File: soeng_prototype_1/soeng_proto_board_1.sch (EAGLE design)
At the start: 11 parts, among them J1 2172034-1

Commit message: PCB Rev. 2
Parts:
- removed CN1: (no value), adafruit:JST_2PIN-THM-RA
- added R1: 10, adafruit:R-US_0207/9
- added SPKR+, SPKR-: WIREPAD1,6/0,8, wirepad:WIREPAD1,6/0,8
- added T1: 2N2222, adafruit:2N2222
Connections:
- new net N$9: R1.1, SPKR+.P
- net +5V: now also T1.C
- net GND: now also SPKR-.P
- net N$4: now also T1.B; no longer CN1.2
- net N$6: now also R1.2, T1.E; no longer CN1.1, U$1.AUD_N
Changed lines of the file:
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@@
 <part name="J1" library="TE-Mini-USB" deviceset="2172034-1" device=""/>
 <part name="LED_STRIP" library="pinhead" library_urn="urn:adsk.eagle:library:325" deviceset="PINHD-1X3" device="" package3d_urn="urn:adsk.eagle:package:22458/2"/>
-<part name="CN1" library="adafruit" library_urn="urn:adsk.eagle:library:420" deviceset="JST_2PIN" device="-THM-RA" package3d_urn="urn:adsk.eagle:package:6240694/1"/>
 <part name="U$2" library="lap_2019" deviceset="RDI-PUSHBUTTON" device=""/>
 <part name="U$3" library="lap_2019" deviceset="RDI-PUSHBUTTON" device=""/>
@@
 <part name="C4" library="adafruit" library_urn="urn:adsk.eagle:library:420" deviceset="C-US" device="025-025X050" package3d_urn="urn:adsk.eagle:package:6240323/1"/>
 <part name="DOT_MATRIX_DISPLAY" library="pinhead" library_urn="urn:adsk.eagle:library:325" deviceset="PINHD-1X5" device="" package3d_urn="urn:adsk.eagle:package:22469/2"/>
+<part name="T1" library="adafruit" library_urn="urn:adsk.eagle:library:420" deviceset="2N2222" device="" package3d_urn="urn:adsk.eagle:package:6240647/1"/>
+<part name="SPKR+" library="wirepad" library_urn="urn:adsk.eagle:library:412" deviceset="WIREPAD" device="1,6/0,8" package3d_urn="urn:adsk.eagle:package:30830/1"/>
+<part name="SPKR-" library="wirepad" library_urn="urn:adsk.eagle:library:412" deviceset="WIREPAD" device="1,6/0,8" package3d_urn="urn:adsk.eagle:package:30830/1"/>
+<part name="R1" library="adafruit" library_urn="urn:adsk.eagle:library:420" deviceset="R-US_" device="0207/9" package3d_urn="urn:adsk.eagle:package:6240935/1" value="10"/>
 </parts>
 <sheets>
@@
 <attribute name="VALUE" x="3.81" y="35.56" size="1.778" layer="96" rot="R180"/>
 </instance>
-<instance part="CN1" gate="G$1" x="-2.54" y="12.7" smashed="yes" rot="R180">
-<attribute name="NAME" x="3.81" y="6.985" size="1.778" layer="95" rot="R180"/>
-<attribute name="VALUE" x="3.81" y="17.78" size="1.778" layer="96" rot="R180"/>
-</instance>
 <instance part="U$2" gate="G$1" x="35.56" y="-10.16" smashed="yes"/>
 <instance part="U$3" gate="G$1" x="35.56" y="-38.1" smashed="yes"/>
@@
 <attribute name="NAME" x="3.81" y="37.465" size="1.778" layer="95" rot="R180"/>
 <attribute name="VALUE" x="3.81" y="55.88" size="1.778" layer="96" rot="R180"/>
+</instance>
+<instance part="T1" gate="G$1" x="12.7" y="0" smashed="yes">
+<attribute name="NAME" x="2.54" y="7.62" size="1.778" layer="95"/>
+<attribute name="VALUE" x="2.54" y="5.08" size="1.778" layer="96"/>
+</instance>
+<instance part="SPKR+" gate="G$1" x="15.24" y="-22.86" smashed="yes" rot="R90">
+<attribute name="NAME" x="13.3858" y="-24.003" size="1.778" layer="95" rot="R90"/>
+<attribute name="VALUE" x="18.542" y="-24.003" size="1.778" layer="96" rot="R90"/>
+</instance>
+<instance part="SPKR-" gate="G$1" x="15.24" y="-30.48" smashed="yes" rot="R270">
+<attribute name="NAME" x="17.0942" y="-29.337" size="1.778" layer="95" rot="R270"/>
+<attribute name="VALUE" x="11.938" y="-29.337" size="1.778" layer="96" rot="R270"/>
+</instance>
+<instance part="R1" gate="G$1" x="15.24" y="-12.7" smashed="yes" rot="R90">
+<attribute name="NAME" x="13.7414" y="-16.51" size="1.778" layer="95" rot="R90"/>
+<attribute name="VALUE" x="18.542" y="-16.51" size="1.778" layer="96" rot="R90"/>
 </instance>
 </instances>
@@
 <junction x="104.14" y="10.16"/>
 </segment>
+<segment>
+<pinref part="SPKR-" gate="G$1" pin="P"/>
+<wire x1="15.24" y1="-33.02" x2="15.24" y2="-50.8" width="0.1524" layer="91"/>
+<label x="15.24" y="-53.34" size="1.778" layer="95"/>
+</segment>
 </net>
 <net name="+5V" class="0">
@@
 <junction x="114.3" y="17.78"/>
 </segment>
+<segment>
+<pinref part="T1" gate="G$1" pin="C"/>
+<wire x1="15.24" y1="5.08" x2="15.24" y2="7.62" width="0.1524" layer="91"/>
+<label x="15.24" y="7.62" size="1.778" layer="95"/>
+</segment>
 </net>
 <net name="N$5" class="0">
@@
 <net name="N$4" class="0">
 <segment>
-<pinref part="CN1" gate="G$1" pin="2"/>
 <wire x1="0" y1="12.7" x2="22.86" y2="12.7" width="0.1524" layer="91"/>
 <wire x1="22.86" y1="12.7" x2="22.86" y2="35.56" width="0.1524" layer="91"/>
 <pinref part="U$1" gate="G$1" pin="AUD_P"/>
 <wire x1="22.86" y1="35.56" x2="33.02" y2="35.56" width="0.1524" layer="91"/>
-</segment>
-</net>
-<net name="N$6" class="0">
-<segment>
-<pinref part="U$1" gate="G$1" pin="AUD_N"/>
-<wire x1="33.02" y1="33.02" x2="25.4" y2="33.02" width="0.1524" layer="91"/>
-<wire x1="25.4" y1="33.02" x2="25.4" y2="10.16" width="0.1524" layer="91"/>
-<pinref part="CN1" gate="G$1" pin="1"/>
-<wire x1="25.4" y1="10.16" x2="0" y2="10.16" width="0.1524" layer="91"/>
+<pinref part="T1" gate="G$1" pin="B"/>
+<wire x1="10.16" y1="0" x2="0" y2="0" width="0.1524" layer="91"/>
+<wire x1="0" y1="0" x2="0" y2="12.7" width="0.1524" layer="91"/>
 </segment>
 </net>
@@
 </segment>
 </net>
+<net name="N$6" class="0">
+<segment>
+<pinref part="T1" gate="G$1" pin="E"/>
+<pinref part="R1" gate="G$1" pin="2"/>
+<wire x1="15.24" y1="-7.62" x2="15.24" y2="-5.08" width="0.1524" layer="91"/>
+</segment>
+</net>
+<net name="N$9" class="0">
+<segment>
+<pinref part="R1" gate="G$1" pin="1"/>
+<pinref part="SPKR+" gate="G$1" pin="P"/>
+<wire x1="15.24" y1="-17.78" x2="15.24" y2="-20.32" width="0.1524" layer="91"/>
+</segment>
+</net>

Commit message: Rev. 3
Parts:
- removed SPKR+, SPKR-: WIREPAD1,6/0,8, wirepad:WIREPAD1,6/0,8
- added U$4: MICRO_SPKR, lap_2019:MICRO_SPKR
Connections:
- net GND: now also U$4.SPKR-; no longer SPKR-.P
- net N$9: now also U$4.SPKR+; no longer SPKR+.P
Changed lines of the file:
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@@
 <?xml version="1.0" encoding="utf-8"?>
 <!DOCTYPE eagle SYSTEM "eagle.dtd">
-<eagle version="9.5.2">
+<eagle version="9.6.2">
 <drawing>
 <settings>
@@
 <part name="DOT_MATRIX_DISPLAY" library="pinhead" library_urn="urn:adsk.eagle:library:325" deviceset="PINHD-1X5" device="" package3d_urn="urn:adsk.eagle:package:22469/2"/>
 <part name="T1" library="adafruit" library_urn="urn:adsk.eagle:library:420" deviceset="2N2222" device="" package3d_urn="urn:adsk.eagle:package:6240647/1"/>
-<part name="SPKR+" library="wirepad" library_urn="urn:adsk.eagle:library:412" deviceset="WIREPAD" device="1,6/0,8" package3d_urn="urn:adsk.eagle:package:30830/1"/>
-<part name="SPKR-" library="wirepad" library_urn="urn:adsk.eagle:library:412" deviceset="WIREPAD" device="1,6/0,8" package3d_urn="urn:adsk.eagle:package:30830/1"/>
 <part name="R1" library="adafruit" library_urn="urn:adsk.eagle:library:420" deviceset="R-US_" device="0207/9" package3d_urn="urn:adsk.eagle:package:6240935/1" value="10"/>
+<part name="U$4" library="lap_2019" deviceset="MICRO_SPKR" device=""/>
 </parts>
 <sheets>
@@
 <attribute name="VALUE" x="2.54" y="5.08" size="1.778" layer="96"/>
 </instance>
-<instance part="SPKR+" gate="G$1" x="15.24" y="-22.86" smashed="yes" rot="R90">
-<attribute name="NAME" x="13.3858" y="-24.003" size="1.778" layer="95" rot="R90"/>
-<attribute name="VALUE" x="18.542" y="-24.003" size="1.778" layer="96" rot="R90"/>
-</instance>
-<instance part="SPKR-" gate="G$1" x="15.24" y="-30.48" smashed="yes" rot="R270">
-<attribute name="NAME" x="17.0942" y="-29.337" size="1.778" layer="95" rot="R270"/>
-<attribute name="VALUE" x="11.938" y="-29.337" size="1.778" layer="96" rot="R270"/>
-</instance>
 <instance part="R1" gate="G$1" x="15.24" y="-12.7" smashed="yes" rot="R90">
 <attribute name="NAME" x="13.7414" y="-16.51" size="1.778" layer="95" rot="R90"/>
 <attribute name="VALUE" x="18.542" y="-16.51" size="1.778" layer="96" rot="R90"/>
 </instance>
+<instance part="U$4" gate="G$1" x="22.86" y="-53.34" smashed="yes"/>
 </instances>
 <busses>
@@
 </segment>
 <segment>
-<pinref part="SPKR-" gate="G$1" pin="P"/>
-<wire x1="15.24" y1="-33.02" x2="15.24" y2="-50.8" width="0.1524" layer="91"/>
-<label x="15.24" y="-53.34" size="1.778" layer="95"/>
+<pinref part="U$4" gate="G$1" pin="SPKR-"/>
+<wire x1="15.24" y1="-50.8" x2="15.24" y2="-58.42" width="0.1524" layer="91"/>
+<label x="12.7" y="-60.96" size="1.778" layer="95"/>
 </segment>
 </net>
@@
 <segment>
 <pinref part="R1" gate="G$1" pin="1"/>
-<pinref part="SPKR+" gate="G$1" pin="P"/>
-<wire x1="15.24" y1="-17.78" x2="15.24" y2="-20.32" width="0.1524" layer="91"/>
-</segment>
-</net>
+<pinref part="U$4" gate="G$1" pin="SPKR+"/>
+<wire x1="15.24" y1="-17.78" x2="15.24" y2="-43.18" width="0.1524" layer="91"/>
+</segment>
+</net>

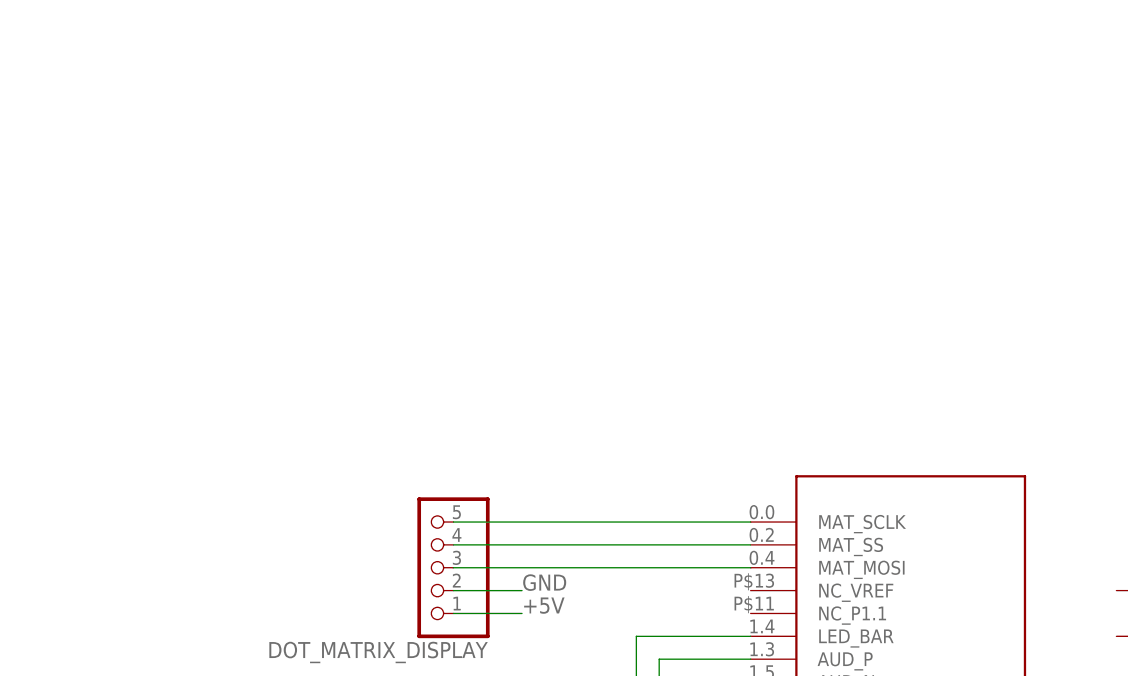
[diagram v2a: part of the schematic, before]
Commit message: Added TCXO, 3.3V Zener, RC
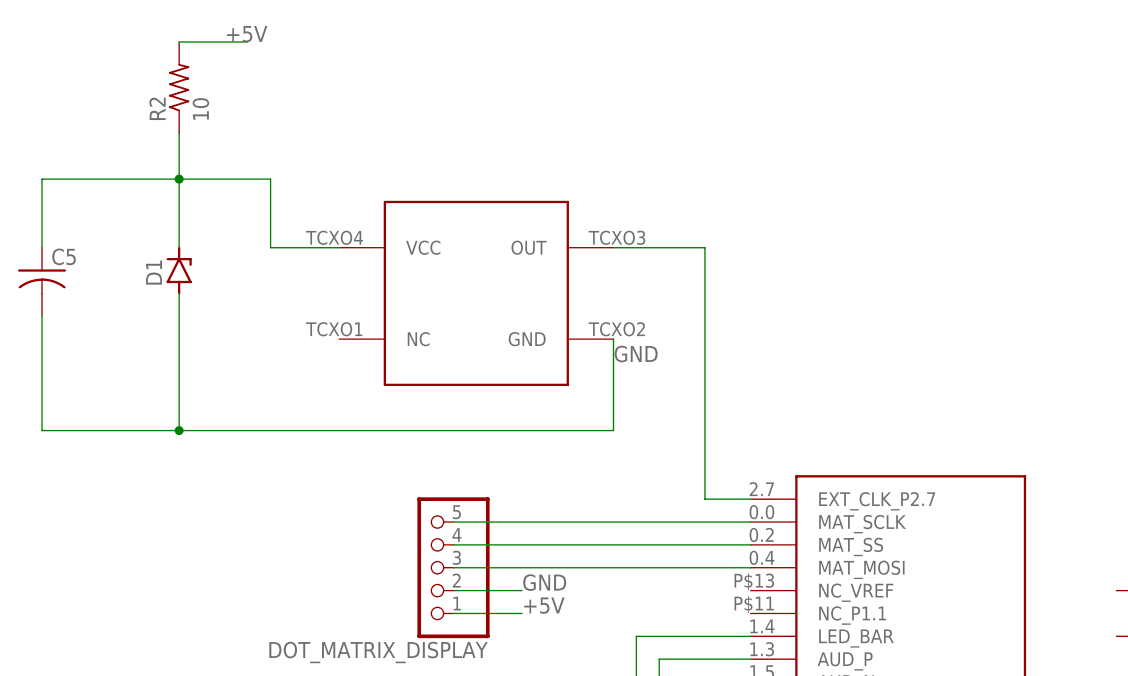
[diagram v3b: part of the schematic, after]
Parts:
- added C5: (no value), adafruit:C-US025-025X050
- added D1: (no value), diode:ZENER-DIODEDO34-7
- added R2: 10, adafruit:R-US_0207/9
- added U$5: TXEAPLSANF, lap_2019:TXEAPLSANF
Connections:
- new net N$10: U$1.EXT_CLK_P2.7, U$5.OUT
- new net N$11: C5.1, D1.C, R2.1, U$5.VCC
- net +5V: now also R2.2
- net GND: now also C5.2, D1.A, U$5.GND
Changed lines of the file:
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@@
 <part name="R1" library="adafruit" library_urn="urn:adsk.eagle:library:420" deviceset="R-US_" device="0207/9" package3d_urn="urn:adsk.eagle:package:6240935/1" value="10"/>
 <part name="U$4" library="lap_2019" deviceset="MICRO_SPKR" device=""/>
+<part name="U$5" library="lap_2019" deviceset="TXEAPLSANF" device=""/>
+<part name="D1" library="diode" library_urn="urn:adsk.eagle:library:210" deviceset="ZENER-DIODE" device="DO34-7" package3d_urn="urn:adsk.eagle:package:43364/1"/>
+<part name="R2" library="adafruit" library_urn="urn:adsk.eagle:library:420" deviceset="R-US_" device="0207/9" package3d_urn="urn:adsk.eagle:package:6240935/1" value="10"/>
+<part name="C5" library="adafruit" library_urn="urn:adsk.eagle:library:420" deviceset="C-US" device="025-025X050" package3d_urn="urn:adsk.eagle:package:6240323/1"/>
 </parts>
 <sheets>
@@
 </instance>
 <instance part="U$4" gate="G$1" x="22.86" y="-53.34" smashed="yes"/>
+<instance part="U$5" gate="G$1" x="2.54" y="76.2" smashed="yes"/>
+<instance part="D1" gate="G$1" x="-30.48" y="78.74" smashed="yes" rot="R90">
+<attribute name="NAME" x="-32.385" y="76.962" size="1.778" layer="95" rot="R90"/>
+<attribute name="VALUE" x="-27.051" y="76.962" size="1.778" layer="96" rot="R90"/>
+</instance>
+<instance part="R2" gate="G$1" x="-30.48" y="99.06" smashed="yes" rot="R90">
+<attribute name="NAME" x="-31.9786" y="95.25" size="1.778" layer="95" rot="R90"/>
+<attribute name="VALUE" x="-27.178" y="95.25" size="1.778" layer="96" rot="R90"/>
+</instance>
+<instance part="C5" gate="G$1" x="-45.72" y="78.74" smashed="yes">
+<attribute name="NAME" x="-44.704" y="79.375" size="1.778" layer="95"/>
+<attribute name="VALUE" x="-44.704" y="74.549" size="1.778" layer="96"/>
+</instance>
 </instances>
 <busses>
@@
 <label x="12.7" y="-60.96" size="1.778" layer="95"/>
 </segment>
+<segment>
+<pinref part="U$5" gate="G$1" pin="GND"/>
+<label x="17.78" y="68.58" size="1.778" layer="95"/>
+<pinref part="D1" gate="G$1" pin="A"/>
+<wire x1="-30.48" y1="76.2" x2="-30.48" y2="60.96" width="0.1524" layer="91"/>
+<wire x1="-30.48" y1="60.96" x2="17.78" y2="60.96" width="0.1524" layer="91"/>
+<wire x1="17.78" y1="60.96" x2="17.78" y2="71.12" width="0.1524" layer="91"/>
+<pinref part="C5" gate="G$1" pin="2"/>
+<wire x1="-45.72" y1="73.66" x2="-45.72" y2="60.96" width="0.1524" layer="91"/>
+<wire x1="-45.72" y1="60.96" x2="-30.48" y2="60.96" width="0.1524" layer="91"/>
+<junction x="-30.48" y="60.96"/>
+</segment>
 </net>
 <net name="+5V" class="0">
@@
 <label x="15.24" y="7.62" size="1.778" layer="95"/>
 </segment>
+<segment>
+<pinref part="R2" gate="G$1" pin="2"/>
+<wire x1="-30.48" y1="104.14" x2="-22.86" y2="104.14" width="0.1524" layer="91"/>
+<label x="-25.4" y="104.14" size="1.778" layer="95"/>
+</segment>
 </net>
 <net name="N$5" class="0">
@@
 </segment>
 </net>
+<net name="N$10" class="0">
+<segment>
+<pinref part="U$5" gate="G$1" pin="OUT"/>
+<wire x1="17.78" y1="81.28" x2="27.94" y2="81.28" width="0.1524" layer="91"/>
+<wire x1="27.94" y1="81.28" x2="27.94" y2="53.34" width="0.1524" layer="91"/>
+<pinref part="U$1" gate="G$1" pin="EXT_CLK_P2.7"/>
+<wire x1="27.94" y1="53.34" x2="33.02" y2="53.34" width="0.1524" layer="91"/>
+</segment>
+</net>
+<net name="N$11" class="0">
+<segment>
+<pinref part="R2" gate="G$1" pin="1"/>
+<pinref part="D1" gate="G$1" pin="C"/>
+<wire x1="-30.48" y1="93.98" x2="-30.48" y2="88.9" width="0.1524" layer="91"/>
+<pinref part="C5" gate="G$1" pin="1"/>
+<wire x1="-30.48" y1="88.9" x2="-30.48" y2="81.28" width="0.1524" layer="91"/>
+<wire x1="-45.72" y1="81.28" x2="-45.72" y2="88.9" width="0.1524" layer="91"/>
+<wire x1="-45.72" y1="88.9" x2="-30.48" y2="88.9" width="0.1524" layer="91"/>
+<junction x="-30.48" y="88.9"/>
+<pinref part="U$5" gate="G$1" pin="VCC"/>
+<wire x1="-12.7" y1="81.28" x2="-20.32" y2="81.28" width="0.1524" layer="91"/>
+<wire x1="-20.32" y1="81.28" x2="-20.32" y2="88.9" width="0.1524" layer="91"/>
+<wire x1="-20.32" y1="88.9" x2="-30.48" y2="88.9" width="0.1524" layer="91"/>
+</segment>
+</net>

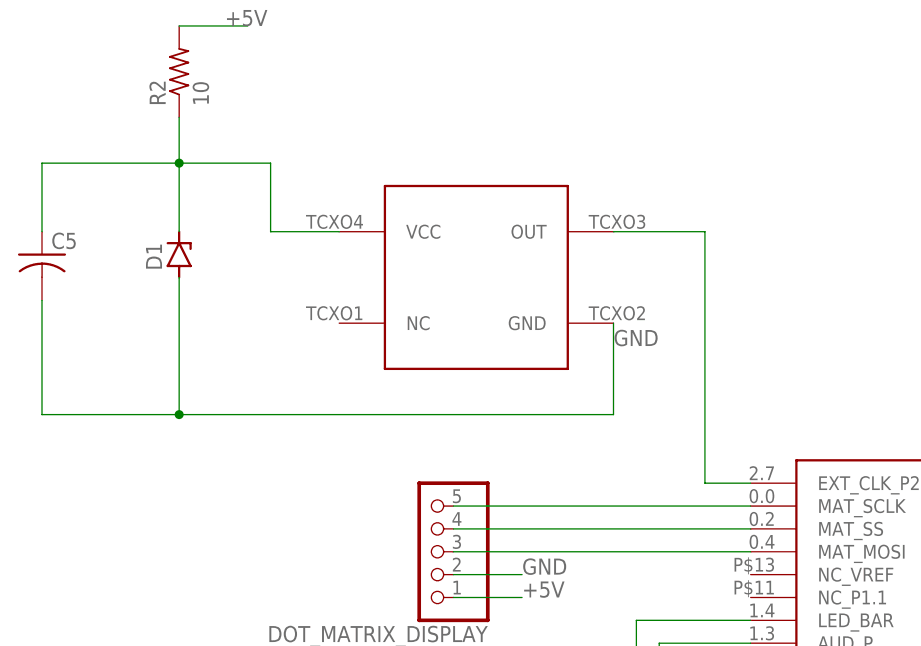
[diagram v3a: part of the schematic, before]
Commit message: Added TCXO, 3.3V Zener, RC
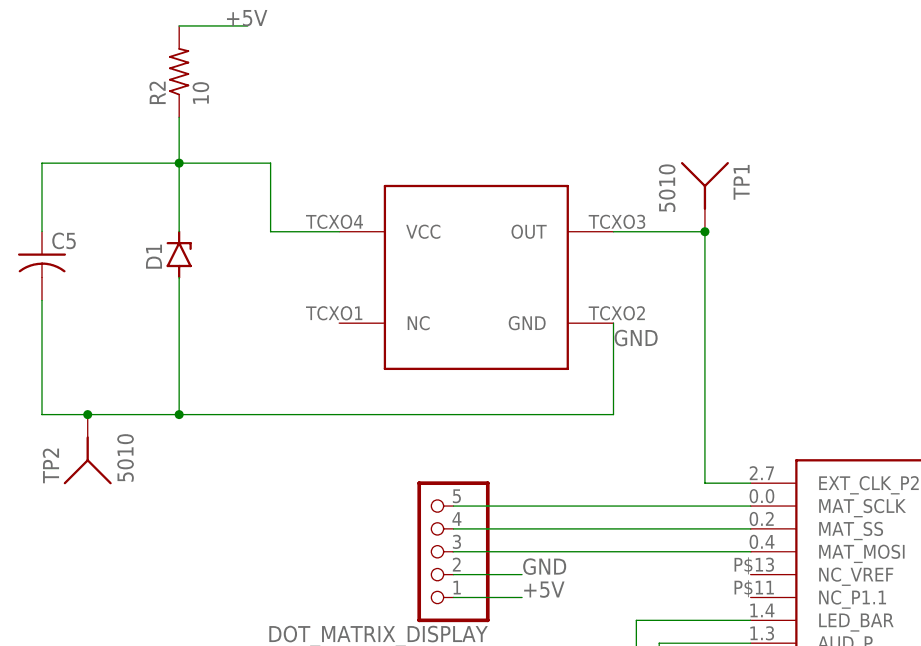
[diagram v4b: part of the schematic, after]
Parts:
- added TP1, TP2: 5010, 5010:5010
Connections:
- net GND: now also TP2.1
- net N$10: now also TP1.1
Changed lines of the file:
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@@
 <part name="R2" library="adafruit" library_urn="urn:adsk.eagle:library:420" deviceset="R-US_" device="0207/9" package3d_urn="urn:adsk.eagle:package:6240935/1" value="10"/>
 <part name="C5" library="adafruit" library_urn="urn:adsk.eagle:library:420" deviceset="C-US" device="025-025X050" package3d_urn="urn:adsk.eagle:package:6240323/1"/>
+<part name="TP1" library="5010" deviceset="5010" device=""/>
+<part name="TP2" library="5010" deviceset="5010" device=""/>
 </parts>
 <sheets>
@@
 <attribute name="NAME" x="-44.704" y="79.375" size="1.778" layer="95"/>
 <attribute name="VALUE" x="-44.704" y="74.549" size="1.778" layer="96"/>
+</instance>
+<instance part="TP1" gate="G$1" x="27.94" y="86.36" smashed="yes" rot="R270">
+<attribute name="NAME" x="31.121959375" y="88.90556875" size="1.781890625" layer="95" rot="R270"/>
+<attribute name="VALUE" x="22.84921875" y="88.905390625" size="1.78178125" layer="96" rot="R270"/>
+</instance>
+<instance part="TP2" gate="G$1" x="-40.64" y="55.88" smashed="yes" rot="R90">
+<attribute name="NAME" x="-43.821959375" y="53.33443125" size="1.781890625" layer="95" rot="R90"/>
+<attribute name="VALUE" x="-35.54921875" y="53.334609375" size="1.78178125" layer="96" rot="R90"/>
 </instance>
 </instances>
@@
 <pinref part="C5" gate="G$1" pin="2"/>
 <wire x1="-45.72" y1="73.66" x2="-45.72" y2="60.96" width="0.1524" layer="91"/>
-<wire x1="-45.72" y1="60.96" x2="-30.48" y2="60.96" width="0.1524" layer="91"/>
+<wire x1="-45.72" y1="60.96" x2="-40.64" y2="60.96" width="0.1524" layer="91"/>
 <junction x="-30.48" y="60.96"/>
+<pinref part="TP2" gate="G$1" pin="1"/>
+<wire x1="-40.64" y1="60.96" x2="-30.48" y2="60.96" width="0.1524" layer="91"/>
+<junction x="-40.64" y="60.96"/>
 </segment>
 </net>
@@
 <pinref part="U$1" gate="G$1" pin="EXT_CLK_P2.7"/>
 <wire x1="27.94" y1="53.34" x2="33.02" y2="53.34" width="0.1524" layer="91"/>
-</segment>
-</net>
+<pinref part="TP1" gate="G$1" pin="1"/>
+<junction x="27.94" y="81.28"/>
+</segment>
+</net>
